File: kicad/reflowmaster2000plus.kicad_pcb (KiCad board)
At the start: 2 copper layers, 46.6 x 24.1 mm, 21 parts, among them IC1 TLP3063, P1 CONN_8, P2 Toaster, P3 220V, U1 TRIAC, U2 TLC2272

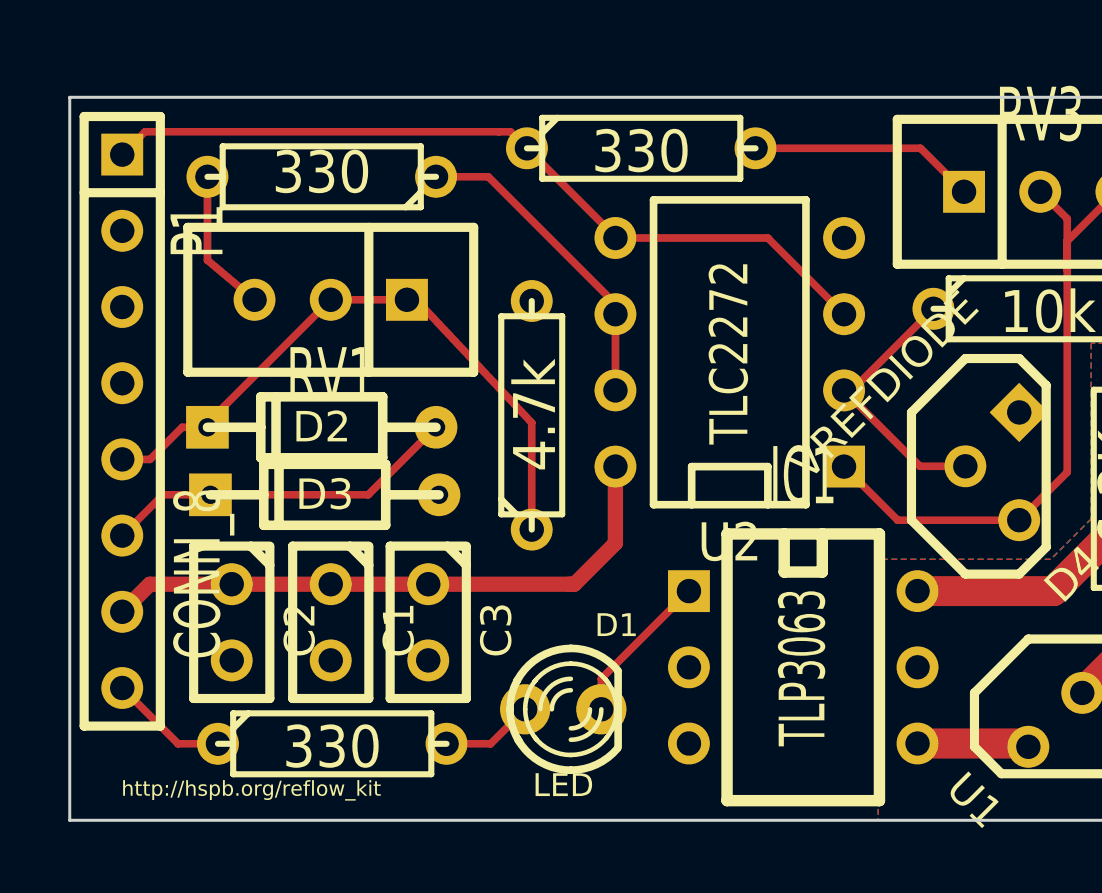
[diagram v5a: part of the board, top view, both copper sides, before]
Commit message: [enh] merged schema blocks into one
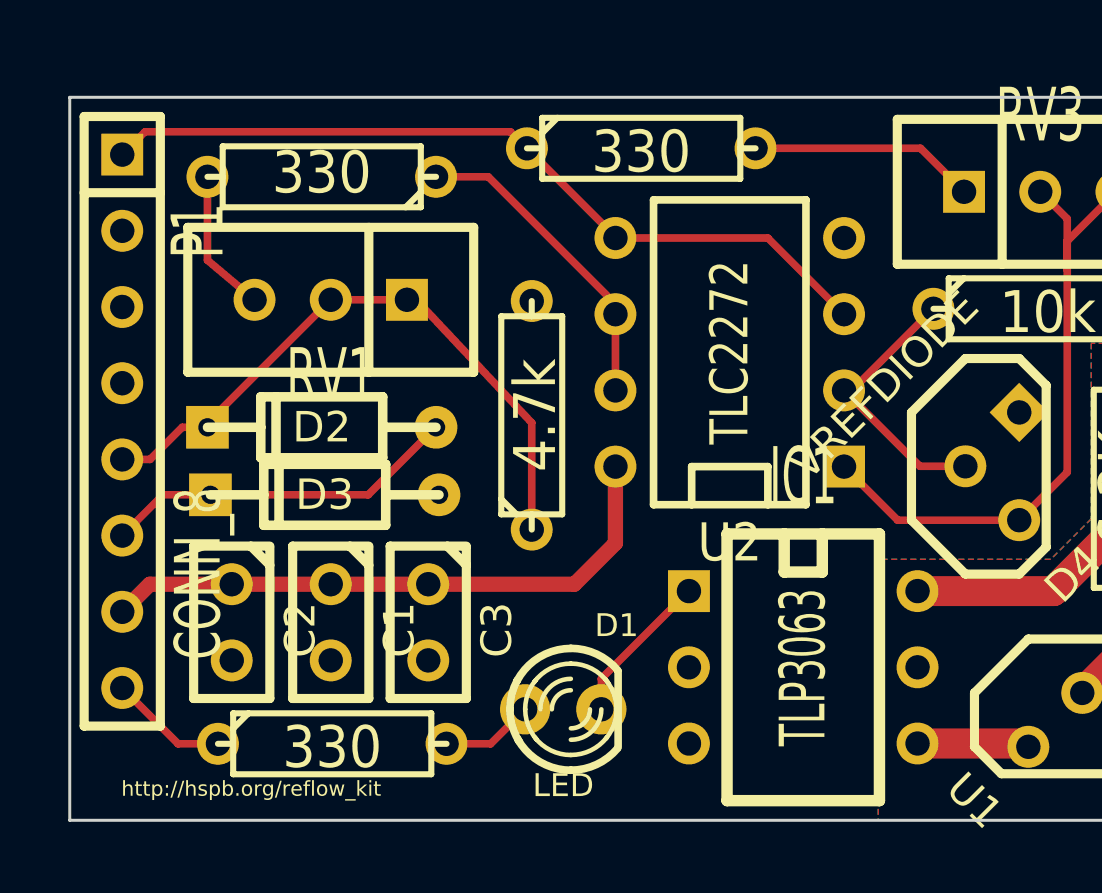
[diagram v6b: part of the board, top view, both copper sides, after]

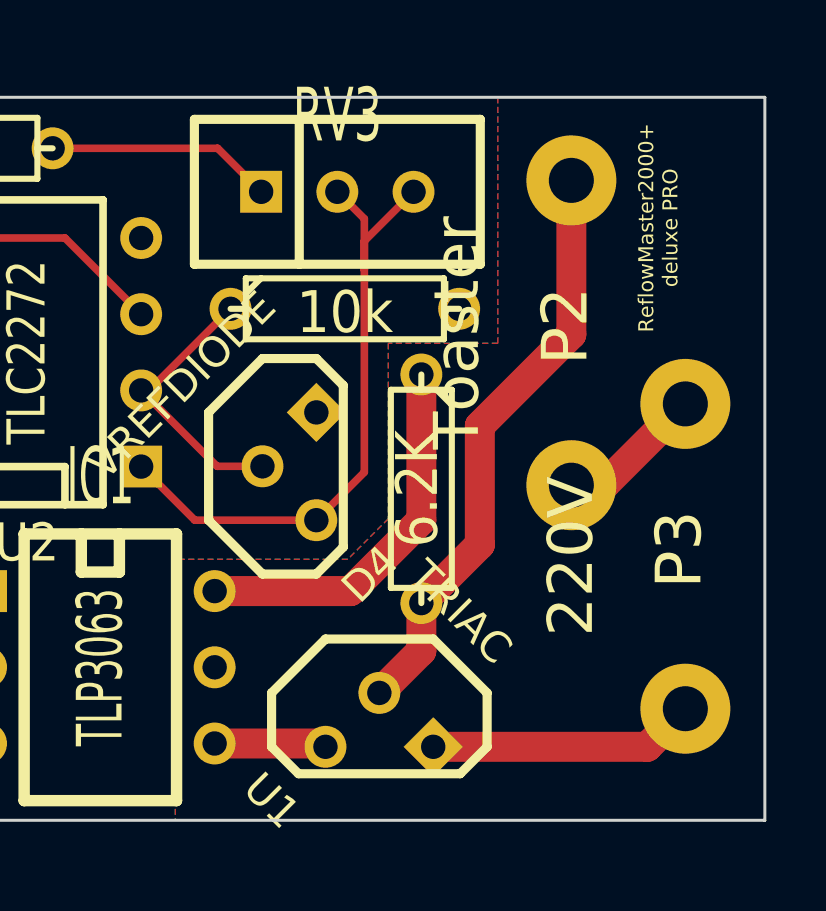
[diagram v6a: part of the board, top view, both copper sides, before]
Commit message: [fix] triac is to220_vert now
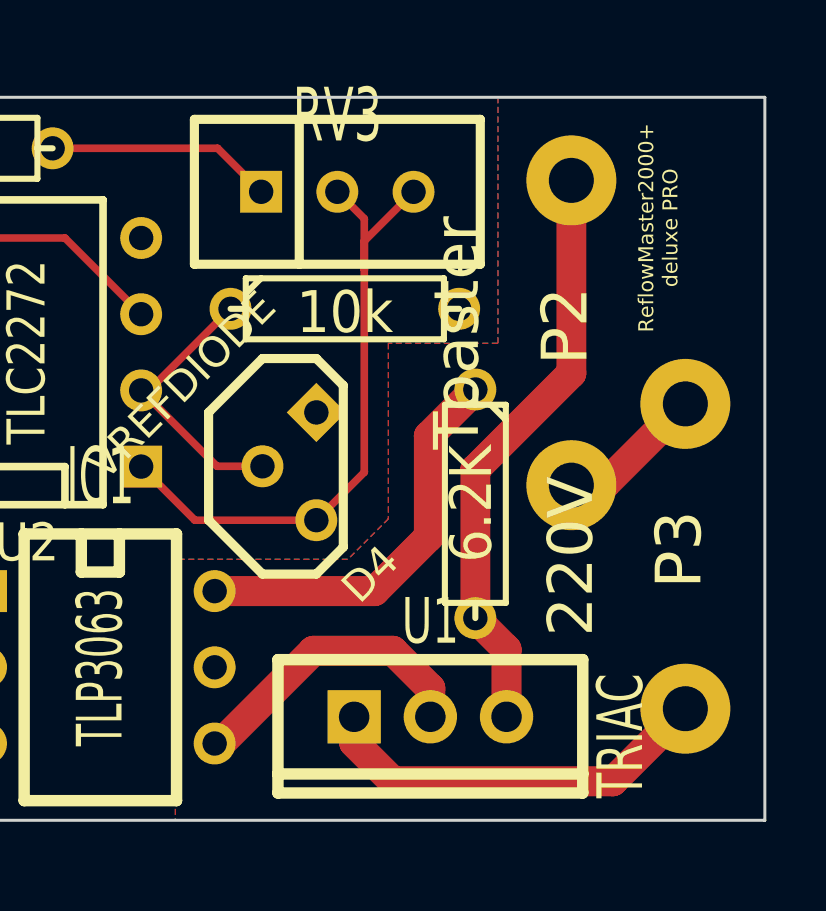
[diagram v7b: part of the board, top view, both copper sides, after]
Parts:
- U1: footprint TO92 -> TO220_VERT
- moved U1 1.97 mm to (190.6, 139.8), turned to 270 degrees
- moved R1 1.87 mm to (192.1, 132.8)
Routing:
- net N-000009: track 3.74 -> 9.94 mm
- net N-0000010: track 8.93 -> 13.4 mm
- net N-000007: track 12.7 -> 13.5 mm
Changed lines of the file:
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@@
     (thickness 1.6)
     (drawings 8)
-    (tracks 71)
+    (tracks 76)
     (zones 0)
     (modules 21)
@@
     (add_net /Utemp)
     (add_net GND)
-    (add_net N-0000010)
     (add_net N-0000013)
     (add_net N-0000016)
-    (add_net N-0000018)
     (add_net N-000003)
     (add_net N-000006)
-    (add_net N-000007)
   )
   (net_class hvpwr ""
@@
     (uvia_drill 0.127)
     (add_net GNDPWR)
+    (add_net N-0000010)
     (add_net N-0000011)
     (add_net N-0000017)
+    (add_net N-0000018)
     (add_net N-000005)
+    (add_net N-000007)
     (add_net N-000009)
   )
@@
       (layers *.Cu *.Mask F.SilkS)
       (net 7 GNDPWR)
-    )
-  )
-  (module TO92 (layer F.Cu)
-    (at 188.85 140.85 315)
-    (descr "Transistor TO92 brochage type BC237")
-    (tags "TR TO92")
-    (fp_text reference U1 (at -1.27 3.81 315) (layer F.SilkS)
-      (effects (font (size 1.016 1.016) (thickness 0.2032)))
-    )
-    (fp_text value TRIAC (at -1.27 -5.08 315) (layer F.SilkS)
-      (effects (font (size 1.016 1.016) (thickness 0.2032)))
-    )
-    (fp_line (start -1.27 2.54) (end 2.54 -1.27) (layer F.SilkS) (width 0.3048))
-    (fp_line (start 2.54 -1.27) (end 2.54 -2.54) (layer F.SilkS) (width 0.3048))
-    (fp_line (start 2.54 -2.54) (end 1.27 -3.81) (layer F.SilkS) (width 0.3048))
-    (fp_line (start 1.27 -3.81) (end -1.27 -3.81) (layer F.SilkS) (width 0.3048))
-    (fp_line (start -1.27 -3.81) (end -3.81 -1.27) (layer F.SilkS) (width 0.3048))
-    (fp_line (start -3.81 -1.27) (end -3.81 1.27) (layer F.SilkS) (width 0.3048))
-    (fp_line (start -3.81 1.27) (end -2.54 2.54) (layer F.SilkS) (width 0.3048))
-    (fp_line (start -2.54 2.54) (end -1.27 2.54) (layer F.SilkS) (width 0.3048))
-    (pad 1 thru_hole rect (at 1.27 -1.27 315) (size 1.397 1.397) (drill 0.8128)
-      (layers *.Cu *.Mask F.SilkS)
-      (net 8 N-0000010)
-    )
-    (pad 2 thru_hole circle (at -1.27 -1.27 315) (size 1.397 1.397) (drill 0.8128)
-      (layers *.Cu *.Mask F.SilkS)
-      (net 13 N-0000018)
-    )
-    (pad 3 thru_hole circle (at -1.27 1.27 315) (size 1.397 1.397) (drill 0.8128)
-      (layers *.Cu *.Mask F.SilkS)
-      (net 18 N-000009)
-    )
-    (model discret/to98.wrl
-      (at (xyz 0 0 0))
-      (scale (xyz 1 1 1))
-      (rotate (xyz 0 0 0))
     )
   )
@@
   )
   (module R3 (layer F.Cu)
-    (at 190.25 132.25 270)
+    (at 192.05 132.75 270)
     (descr "Resitance 3 pas")
     (tags R)
@@
       (layers *.Cu *.Mask F.SilkS)
       (net 3 /PWRctrl)
+    )
+  )
+  (module TO220_VERT (layer F.Cu)
+    (at 190.55 139.85 270)
+    (descr "Regulateur TO220 serie LM78xx")
+    (tags "TR TO220")
+    (fp_text reference U1 (at -3.175 0 360) (layer F.SilkS)
+      (effects (font (size 1.524 1.016) (thickness 0.2032)))
+    )
+    (fp_text value TRIAC (at 0.635 -6.35 270) (layer F.SilkS)
+      (effects (font (size 1.524 1.016) (thickness 0.2032)))
+    )
+    (fp_line (start 1.905 -5.08) (end 2.54 -5.08) (layer F.SilkS) (width 0.381))
+    (fp_line (start 2.54 -5.08) (end 2.54 5.08) (layer F.SilkS) (width 0.381))
+    (fp_line (start 2.54 5.08) (end 1.905 5.08) (layer F.SilkS) (width 0.381))
+    (fp_line (start -1.905 -5.08) (end 1.905 -5.08) (layer F.SilkS) (width 0.381))
+    (fp_line (start 1.905 -5.08) (end 1.905 5.08) (layer F.SilkS) (width 0.381))
+    (fp_line (start 1.905 5.08) (end -1.905 5.08) (layer F.SilkS) (width 0.381))
+    (fp_line (start -1.905 5.08) (end -1.905 -5.08) (layer F.SilkS) (width 0.381))
+    (pad 2 thru_hole circle (at 0 -2.54 270) (size 1.778 1.778) (drill 1.016)
+      (layers *.Cu *.Mask F.SilkS)
+      (net 13 N-0000018)
+    )
+    (pad 3 thru_hole circle (at 0 0 270) (size 1.778 1.778) (drill 1.016)
+      (layers *.Cu *.Mask F.SilkS)
+      (net 18 N-000009)
+    )
+    (pad 1 thru_hole rect (at 0 2.54 270) (size 1.778 1.778) (drill 1.016)
+      (layers *.Cu *.Mask F.SilkS)
+      (net 8 N-0000010)
     )
   )
@@
   (segment (start 195.25 132.13) (end 196.34 132.13) (width 1) (layer F.Cu) (net 7) (status 30))
   (segment (start 196.34 132.13) (end 199.05 129.42) (width 1) (layer F.Cu) (net 7) (status 30))
-  (segment (start 190.646051 140.85) (end 197.78 140.85) (width 1) (layer F.Cu) (net 8) (status 10))
-  (segment (start 197.78 140.85) (end 199.05 139.58) (width 1) (layer F.Cu) (net 8) (status 20))
+  (segment (start 188.01 139.85) (end 188.01 140.71) (width 1) (layer F.Cu) (net 8))
+  (segment (start 196.63 142) (end 199.05 139.58) (width 1) (layer F.Cu) (net 8))
+  (segment (start 189.3 142) (end 196.63 142) (width 1) (layer F.Cu) (net 8))
+  (segment (start 188.01 140.71) (end 189.3 142) (width 1) (layer F.Cu) (net 8))
   (segment (start 180.91 128.97) (end 181.17 128.97) (width 0.254) (layer F.Cu) (net 9) (status 30))
   (segment (start 181.17 128.97) (end 183.89 126.25) (width 0.254) (layer F.Cu) (net 9) (status 30))
@@
   (segment (start 177.96 120.9) (end 183.46 120.9) (width 0.254) (layer F.Cu) (net 12) (status 10))
   (segment (start 183.46 120.9) (end 184.91 122.35) (width 0.254) (layer F.Cu) (net 12) (status 20))
-  (segment (start 190.25 136.06) (end 192.2 134.11) (width 1) (layer F.Cu) (net 13) (status 10))
-  (segment (start 192.2 134.11) (end 192.2 130.15) (width 1) (layer F.Cu) (net 13))
-  (segment (start 195.25 127.1) (end 195.25 121.97) (width 1) (layer F.Cu) (net 13) (status 20))
-  (segment (start 192.2 130.15) (end 195.25 127.1) (width 1) (layer F.Cu) (net 13))
-  (segment (start 188.85 139.053949) (end 190.25 137.653949) (width 1) (layer F.Cu) (net 13) (status 10))
-  (segment (start 190.25 137.653949) (end 190.25 136.06) (width 1) (layer F.Cu) (net 13) (status 20))
+  (segment (start 192.05 136.56) (end 192.05 131.6) (width 1) (layer F.Cu) (net 13) (status 400000))
+  (segment (start 195.25 128.4) (end 195.25 121.97) (width 1) (layer F.Cu) (net 13) (status 800000))
+  (segment (start 192.05 131.6) (end 195.25 128.4) (width 1) (layer F.Cu) (net 13))
+  (segment (start 193.09 139.85) (end 193.09 137.6) (width 1) (layer F.Cu) (net 13) (status 400000))
+  (segment (start 193.09 137.6) (end 192.05 136.56) (width 1) (layer F.Cu) (net 13) (status 800000))
   (segment (start 167.31 121.85) (end 169.05 121.85) (width 0.254) (layer F.Cu) (net 14) (status 10))
   (segment (start 173.29 126.09) (end 173.29 126.43) (width 0.254) (layer F.Cu) (net 14) (status 30))
@@
   (segment (start 169.13 140.75) (end 170.28 139.6) (width 0.254) (layer F.Cu) (net 16) (status 20))
   (segment (start 170.23 139.55) (end 170.28 139.6) (width 0.254) (layer F.Cu) (net 16) (status 30))
-  (segment (start 183.36 135.66) (end 187.89 135.66) (width 1) (layer F.Cu) (net 17) (status 10))
-  (segment (start 187.89 135.66) (end 190.25 133.3) (width 1) (layer F.Cu) (net 17))
-  (segment (start 190.25 133.3) (end 190.25 128.44) (width 1) (layer F.Cu) (net 17) (status 20))
+  (segment (start 183.36 135.66) (end 188.69 135.66) (width 1) (layer F.Cu) (net 17) (status 400000))
+  (segment (start 190.5 130.49) (end 192.05 128.94) (width 1) (layer F.Cu) (net 17) (status 800000))
+  (segment (start 190.5 133.85) (end 190.5 130.49) (width 1) (layer F.Cu) (net 17))
+  (segment (start 188.69 135.66) (end 190.5 133.85) (width 1) (layer F.Cu) (net 17))
   (segment (start 183.37 135.65) (end 183.36 135.66) (width 0.254) (layer F.Cu) (net 17) (status 30))
-  (segment (start 183.36 140.74) (end 186.943949 140.74) (width 1) (layer F.Cu) (net 18) (status 30))
-  (segment (start 186.943949 140.74) (end 187.053949 140.85) (width 1) (layer F.Cu) (net 18) (status 30))
+  (segment (start 190.55 139.85) (end 190.55 138.9) (width 1) (layer F.Cu) (net 18))
+  (segment (start 183.56 140.74) (end 183.36 140.74) (width 1) (layer F.Cu) (net 18))
+  (segment (start 186.65 137.65) (end 183.56 140.74) (width 1) (layer F.Cu) (net 18))
+  (segment (start 189.3 137.65) (end 186.65 137.65) (width 1) (layer F.Cu) (net 18))
+  (segment (start 190.55 138.9) (end 189.3 137.65) (width 1) (layer F.Cu) (net 18))
   (zone (net 6) (net_name GND) (layer F.Cu) (hatch edge 0.508)
     (connect_pads (clearance 0.1))
